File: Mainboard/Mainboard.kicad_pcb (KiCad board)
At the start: 2 copper layers, 60 x 95 mm, 28 parts, among them J1 Bus_M.2_Socket_E, J3 USB_A_Stacked, J4 Micro_SD_Card, J6 Conn_01x09_Pin, J7 Conn_01x09_Pin, U1 Hirose DF40C-100DS-0.4V, U2 ADS1115IDGS, U3 PCM5102, U4 PAM8403D

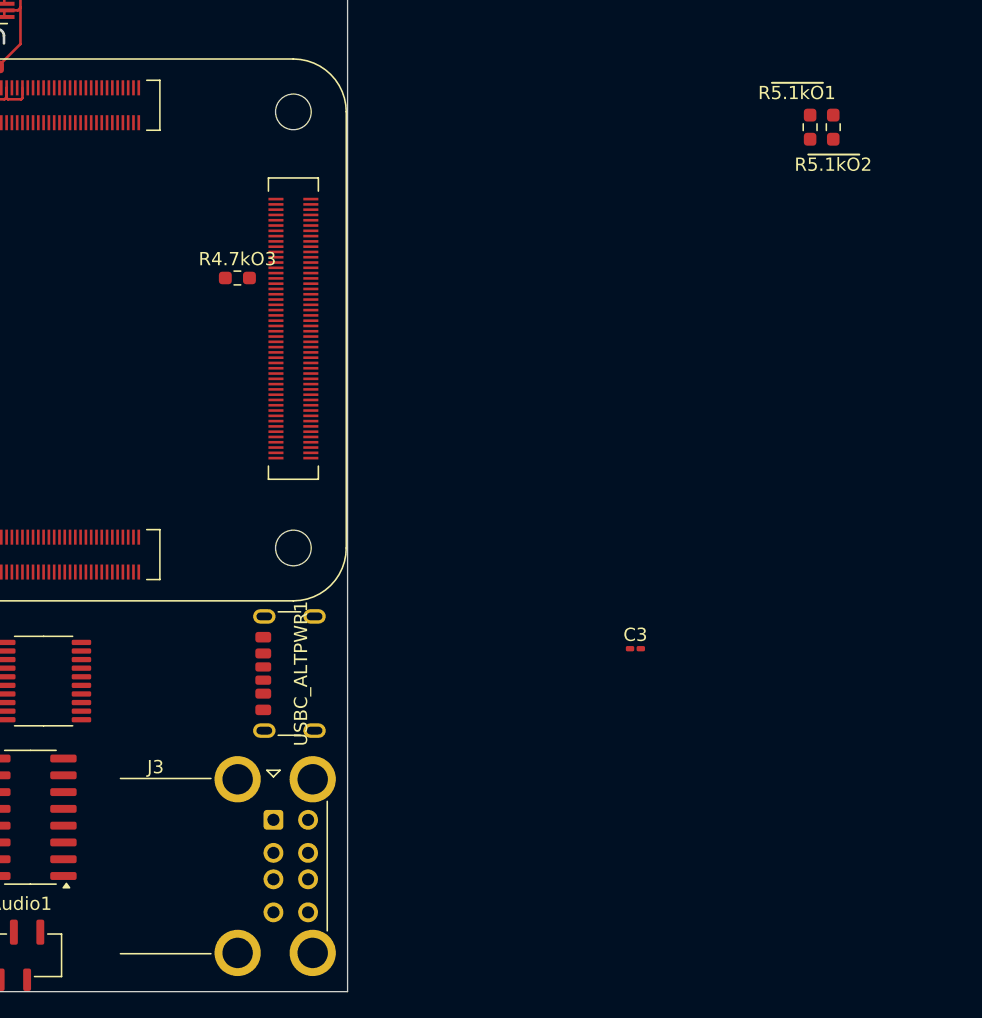
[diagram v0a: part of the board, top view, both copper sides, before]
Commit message: Half Routed USB Tower
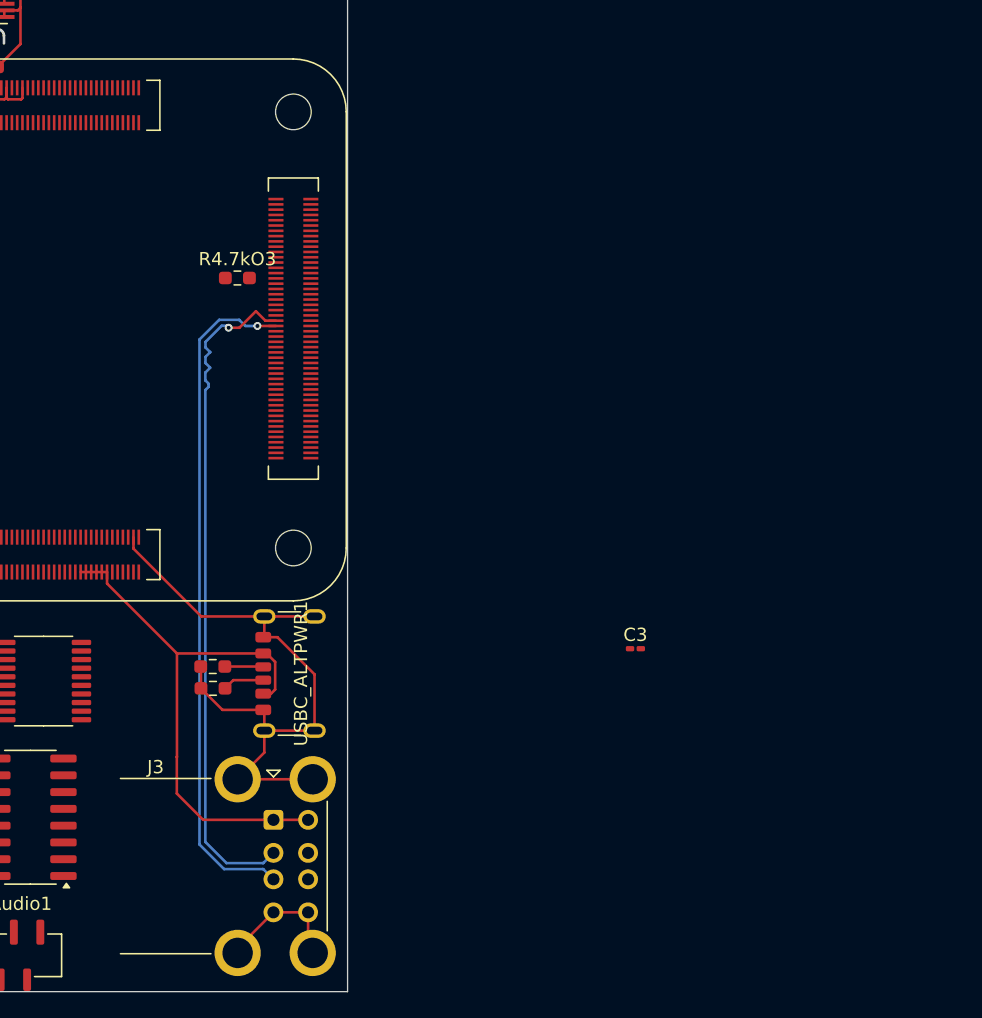
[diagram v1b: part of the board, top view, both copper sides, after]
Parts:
- moved R~{5.1kO}2 62.2 mm to (144.8, 122.9), turned to 0 degrees
- moved R~{5.1kO}1 62.0 mm to (144.8, 124.5), turned to 0 degrees
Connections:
- net Net-(J3-D2+) renamed /USB2_D+
- net Net-(J3-D2-) renamed /USB2_D-
- J3 pad 2: Net-(J3-D1-) -> /USB1_D-
- J3 pad 3: Net-(J3-D1+) -> /USB1_D+
- J3 pad 5: unconnected-(J3-VBUS2-Pad5) -> +5V
- U1 pad 245: Net-(J3-D1+) -> unconnected-(U1C-USB3_HOST1_DP-Pad245)
- U1 pad 247: Net-(J3-D1-) -> unconnected-(U1C-USB3_HOST1_DM-Pad247)
- U1 pad 251: unconnected-(U1C-USB3_HOST1_SSTXP-Pad251) -> /USB1_D+
- U1 pad 253: unconnected-(U1C-USB3_HOST1_SSTXN-Pad253) -> /USB1_D-
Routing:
- net GND: track 89.5 -> 149.8 mm
- net /USB1_D-: track 0.00 -> 51.5 mm, vias 0 -> 1
- net /USB1_D+: track 0.00 -> 51.5 mm, vias 0 -> 1
- net +5V: track 0.00 -> 42.5 mm
- net Net-(USBC_ALTPWR1-CC1): track 0.00 -> 3.15 mm
- net Net-(USBC_ALTPWR1-CC2): track 0.00 -> 2.92 mm

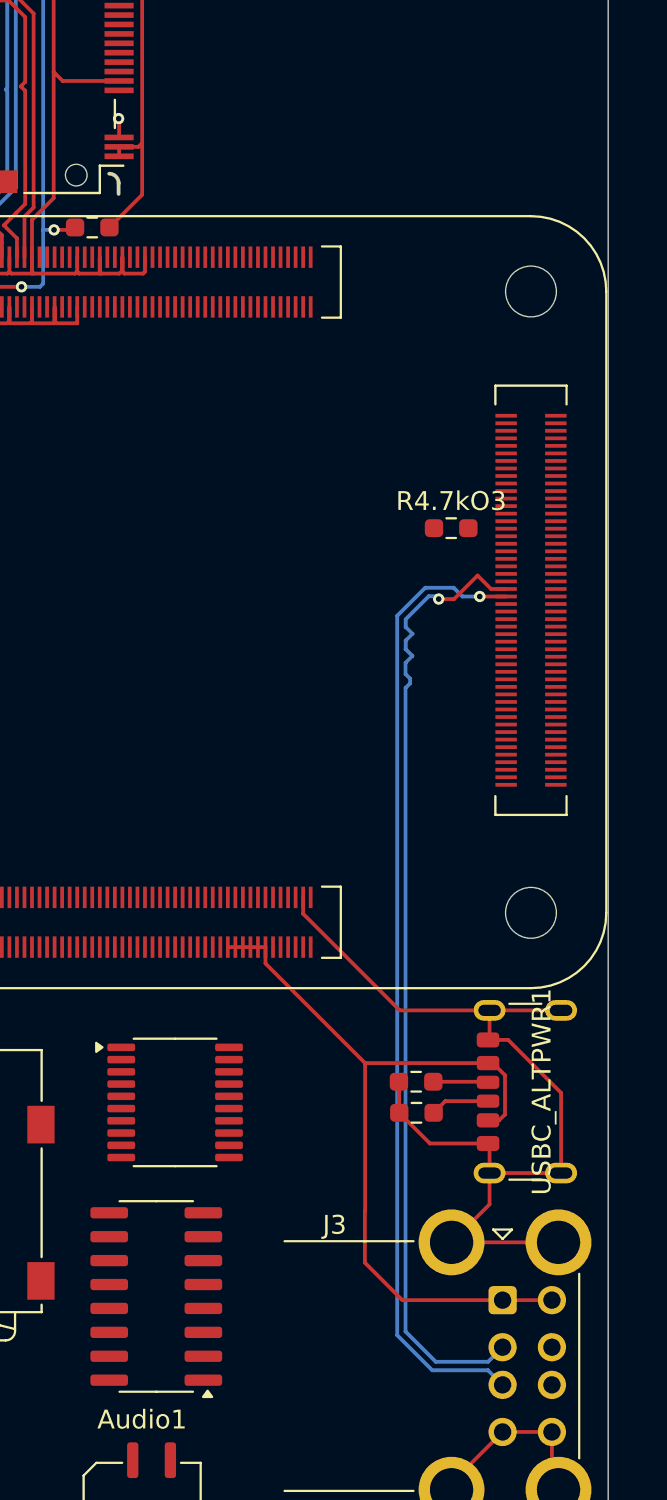
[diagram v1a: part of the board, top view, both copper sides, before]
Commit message: Moved Wifi_LED to GPIO
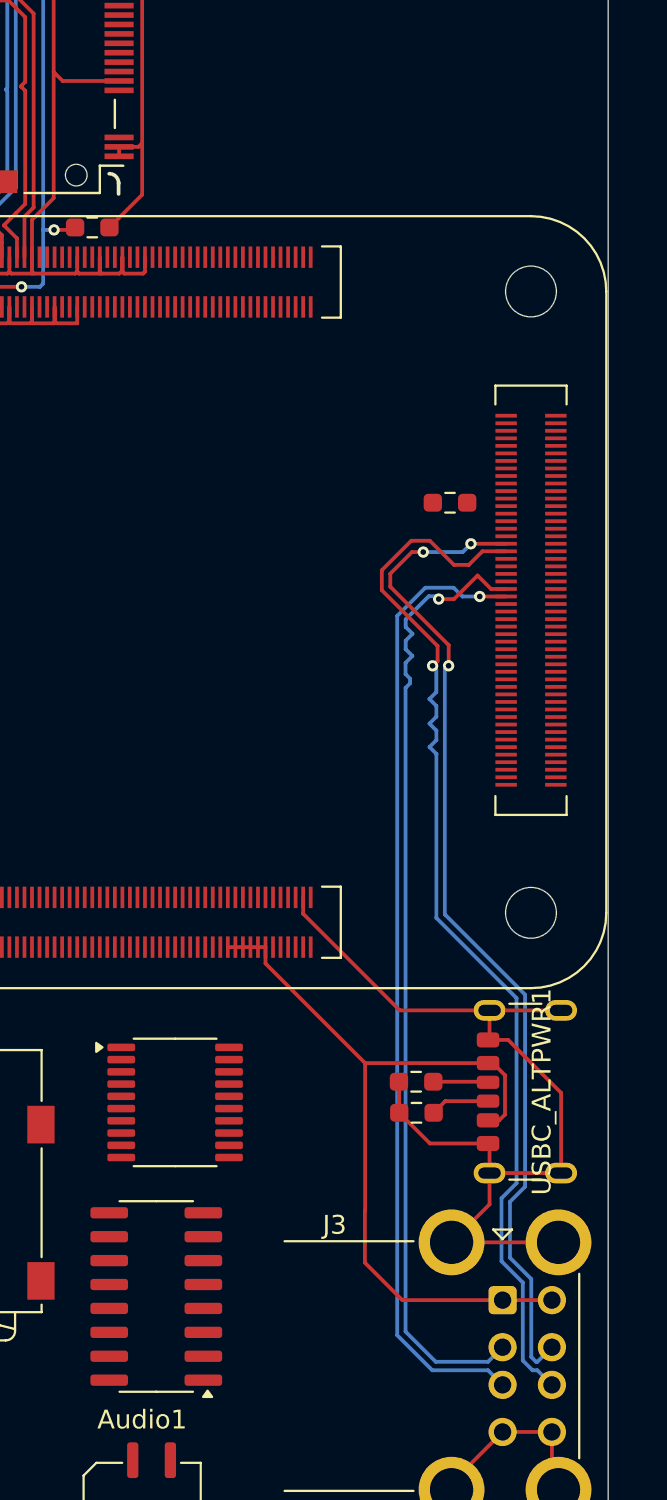
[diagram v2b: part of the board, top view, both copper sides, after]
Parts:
- moved R4.7kO3 1.35 mm to (146.6, 92.2)
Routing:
- net /USB2_D+: track 0.00 -> 57.0 mm, vias 0 -> 1
- net /USB2_D-: track 0.00 -> 53.9 mm, vias 0 -> 3
- net Net-(J1-~{LED_1}): track 1.01 -> 0.00 mm, vias 1 -> 0

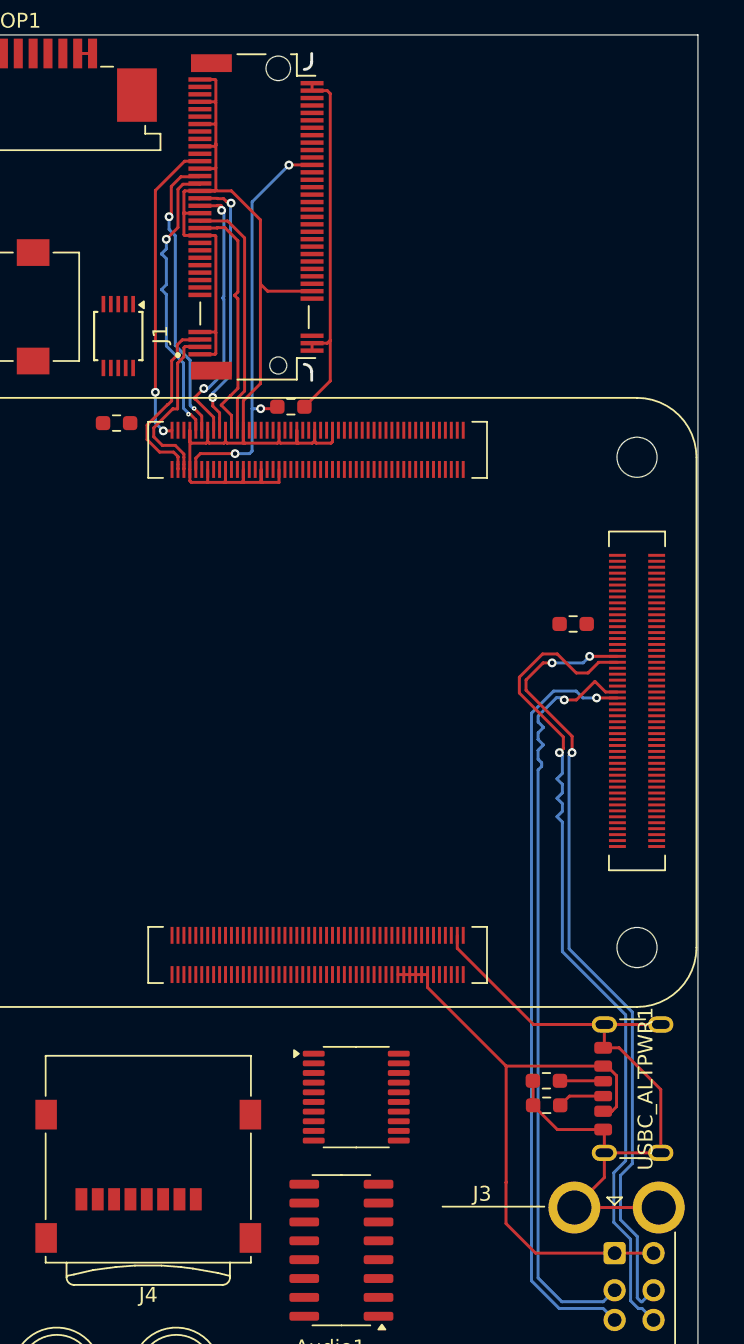
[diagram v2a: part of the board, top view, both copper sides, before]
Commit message: Switch to 4-Layer Setup: F.Cu, In.GND, In.PWR, B.Cu
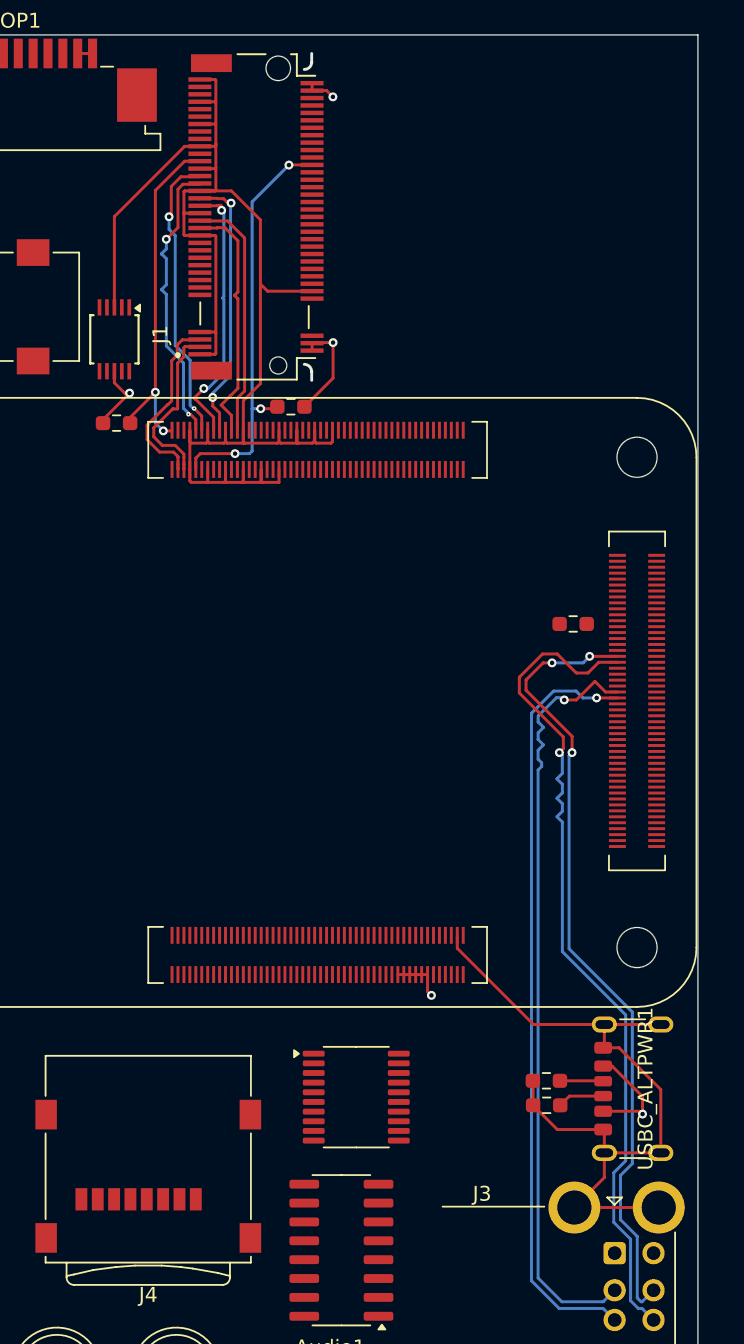
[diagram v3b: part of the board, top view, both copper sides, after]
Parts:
- moved U2 0.34 mm to (115.7, 73.0)
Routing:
- net GND: track 149.8 -> 177.5 mm
- net /3V3: track 26.5 -> 47.3 mm, vias 0 -> 3
- net Net-(J1-~{CLKREQ0}): track 20.8 -> 23.6 mm
- net +5V: track 42.5 -> 42.2 mm, vias 0 -> 2
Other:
- copper layers 2 -> 4

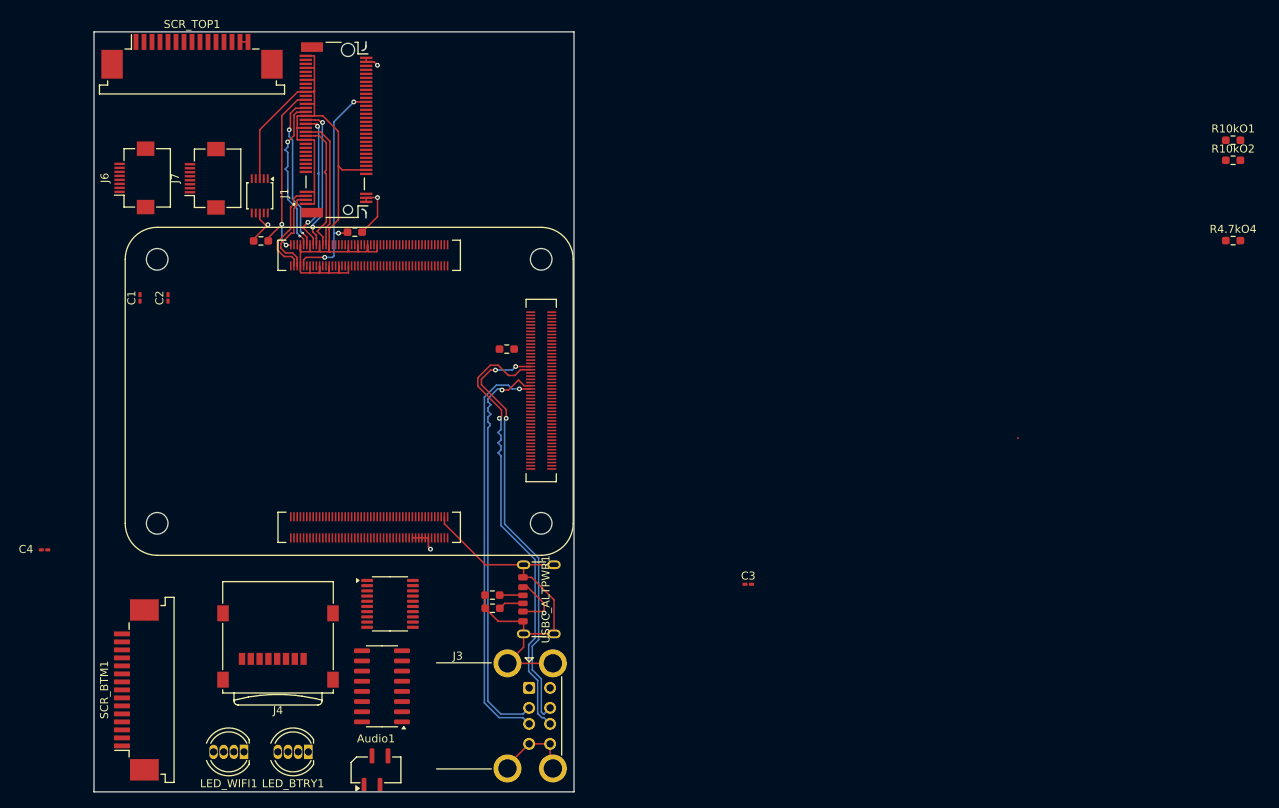
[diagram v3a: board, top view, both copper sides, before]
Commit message: Split Control Setup, -> L & R
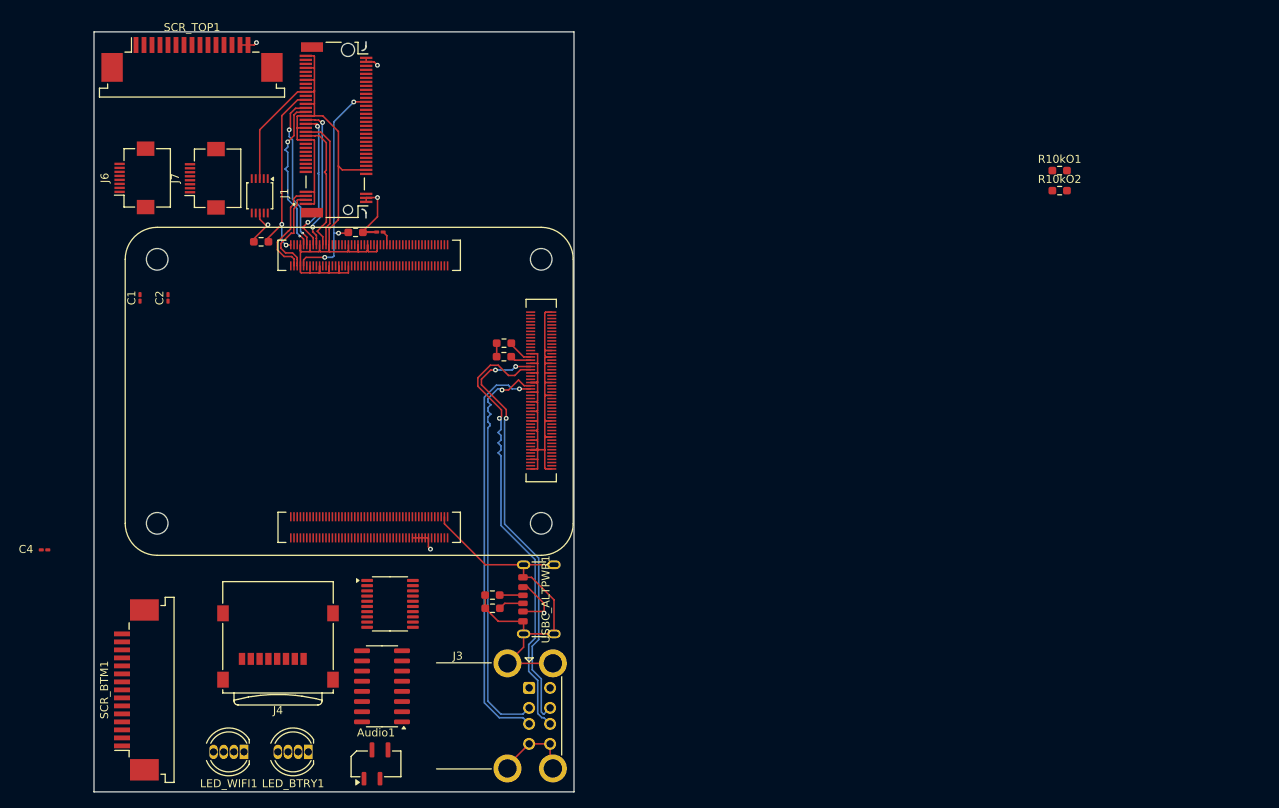
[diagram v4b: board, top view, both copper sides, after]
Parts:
- moved R4.7kO4 92.0 mm to (146.2, 91.4)
- moved C3 63.7 mm to (130.7, 77.5), turned to 180 degrees
- moved R10kO1 22.0 mm to (215.7, 69.8)
- moved R10kO2 22.0 mm to (215.7, 72.3)
- moved R4.7kO1 11.9 mm to (127.7, 77.6), turned to 0 degrees
- moved R4.7kO2 11.8 mm to (115.9, 78.7), turned to 180 degrees
- moved R4.7kO3 1.02 mm to (146.2, 93.1)
- moved Audio1 0.75 mm to (130.2, 144.0)
- moved SCR_TOP1 0.39 mm to (107.2, 55.9)
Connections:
- J1 pad 6: Net-(J1-~{LED_1}) -> unconnected-(J1-~{LED_1}-Pad6)
- LED_WIFI1 pad 1: Net-(J1-~{LED_1}) -> Net-(LED_WIFI1-BA)
- LED_WIFI1 pad 2: Net-(J1-~{LED_1}) -> Net-(LED_WIFI1-GA)
- LED_WIFI1 pad 4: unconnected-(LED_WIFI1-RA-Pad4) -> Net-(LED_WIFI1-RA)
- R4.7kO1 pad 1: Net-(J1-~{CLKREQ0}) -> Net-(J1-~{PERST0})
- R4.7kO2 pad 1: Net-(J1-~{PERST0}) -> Net-(J1-~{CLKREQ0})
- U1 pad 37: unconnected-(U1A-GPIO7-Pad37) -> Net-(LED_WIFI1-RA)
- U1 pad 39: unconnected-(U1A-GPIO8-Pad39) -> Net-(LED_WIFI1-GA)
- U1 pad 41: unconnected-(U1A-GPIO25-Pad41) -> Net-(LED_WIFI1-BA)
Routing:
- net GND: track 177.5 -> 238.6 mm
- net /3V3: track 47.3 -> 71.8 mm, vias 3 -> 4
- net Net-(SCR_BTM1-Pin_12): track 0.00 -> 3.23 mm
- net Net-(SCR_BTM1-Pin_11): track 0.00 -> 2.61 mm
